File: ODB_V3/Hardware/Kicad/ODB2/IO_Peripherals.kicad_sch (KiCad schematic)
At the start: 22 parts, among them J3 SYS_SW_Conn_01x05_Header, J5 RFM_Conn_Coaxial, J6 RFD_Conn_01x05_Header, U10 W25Q512JVEIQ, U9 RFM22B

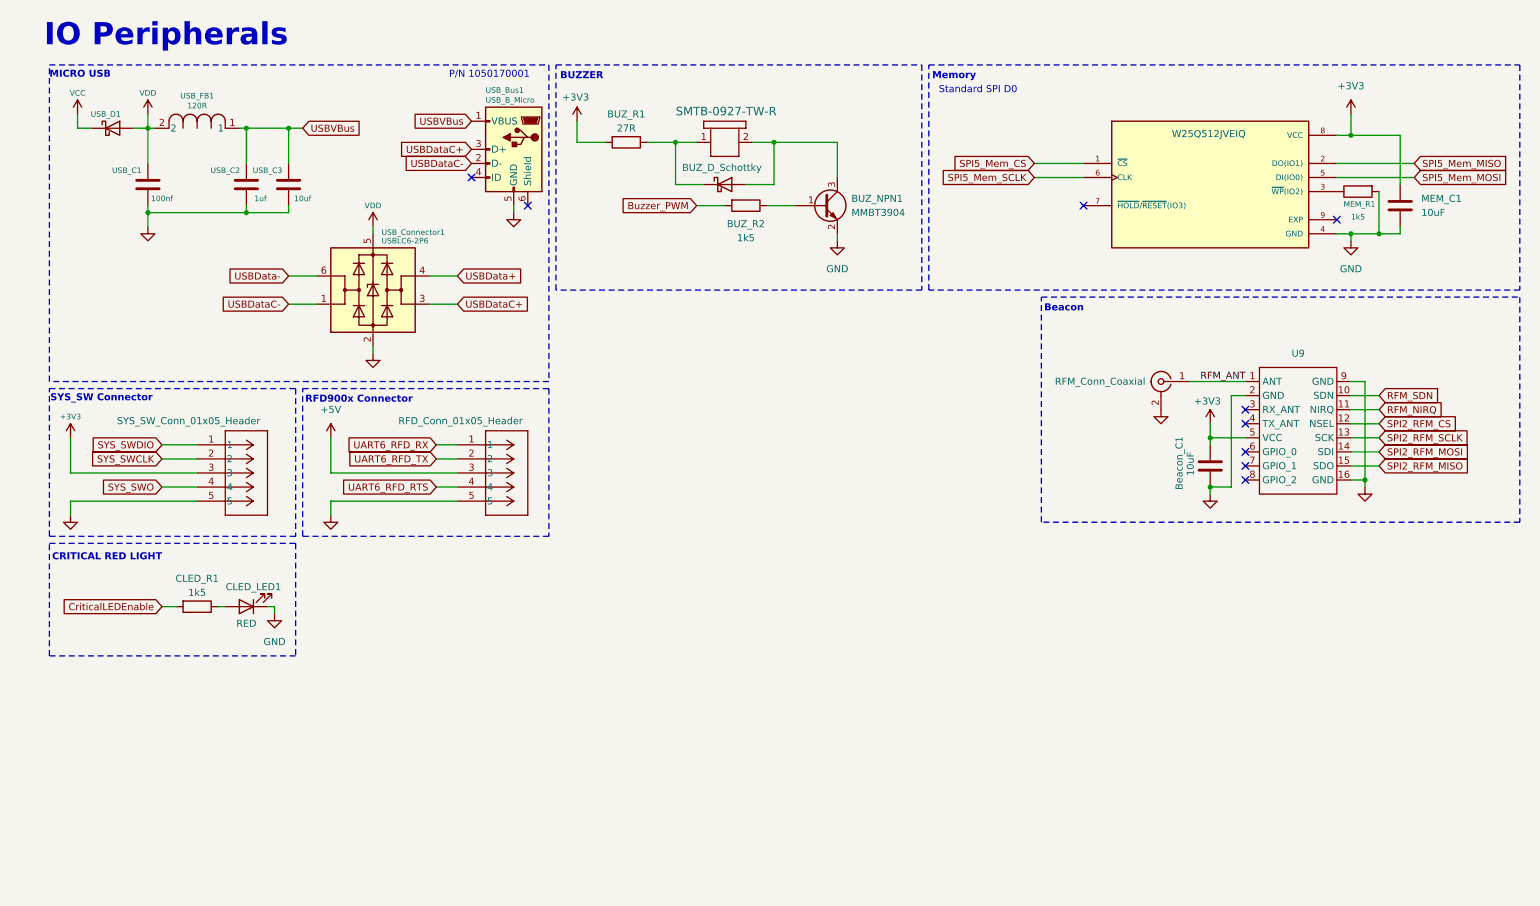
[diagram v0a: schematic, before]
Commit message: feat: new psu design from 5v-36v to 5v (not final)
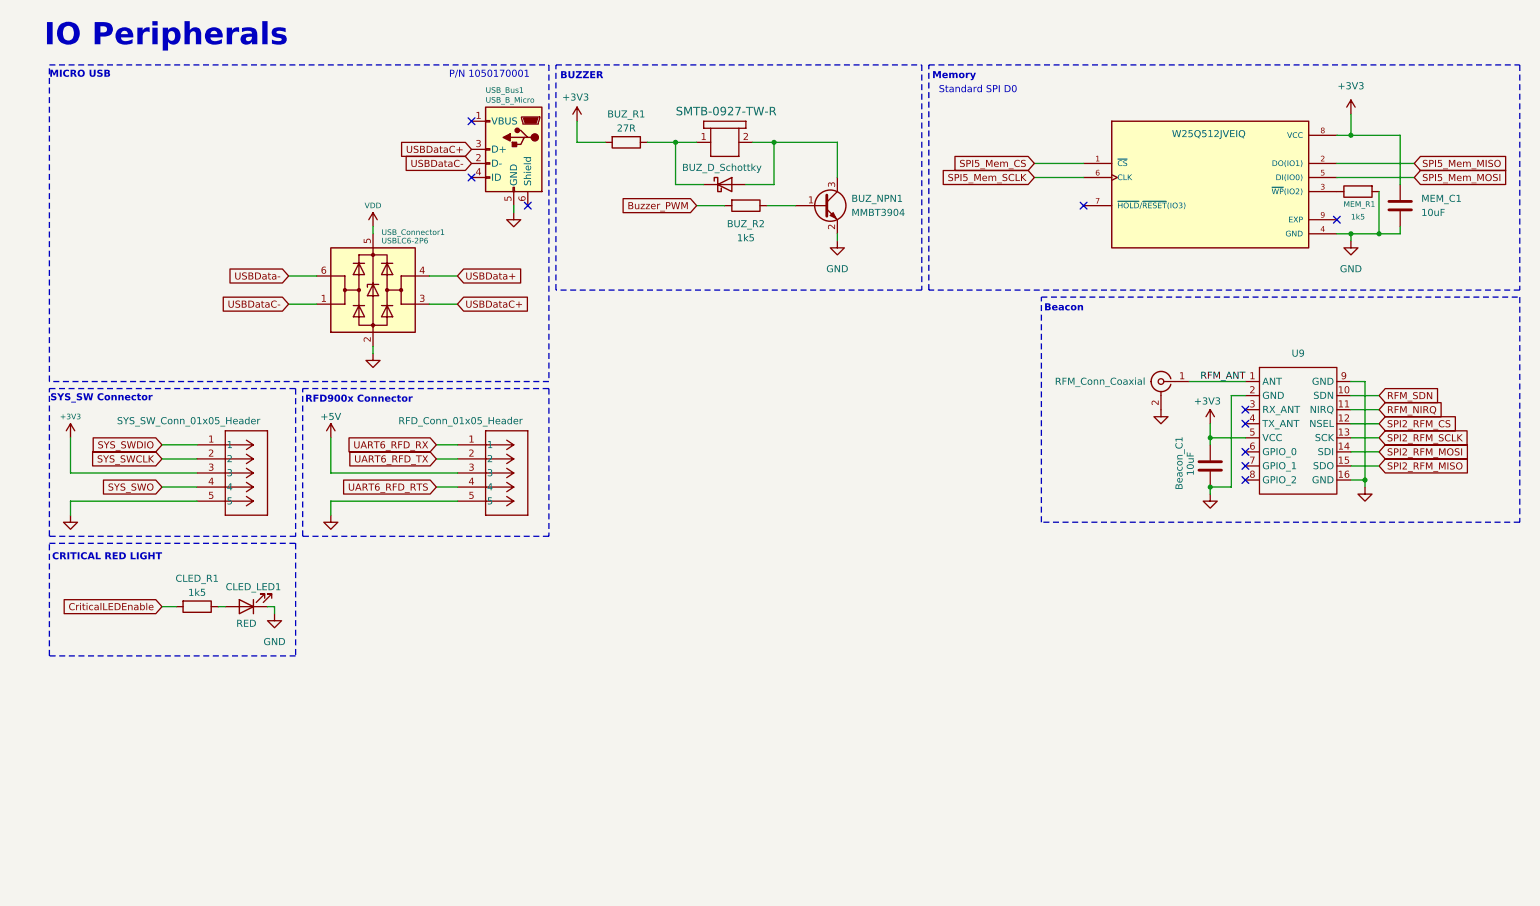
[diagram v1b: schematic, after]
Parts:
- removed USB_C1: 100nf, Capacitor_SMD:C_0603_1608Metric, symbol Device:C
- removed USB_C2: 1uf, Capacitor_SMD:C_0603_1608Metric, symbol Device:C
- removed USB_C3: 10uf, Capacitor_SMD:C_0603_1608Metric, symbol Device:C
- removed USB_D1: B260A-13-F, Diode_SMD:D_SOD-123, symbol Device:D_Schottky
- removed USB_FB1: 120R, IND_25_0805_FRT, symbol ODB2:2508051217Y6
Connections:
- net USBVBus: no longer names the net of USB_Bus1.1 (VBUS)
- no-connect marks 9 -> 10

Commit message: feat!: cleanup components, add new footprint/step, add stm32cubeide conf, start schematics
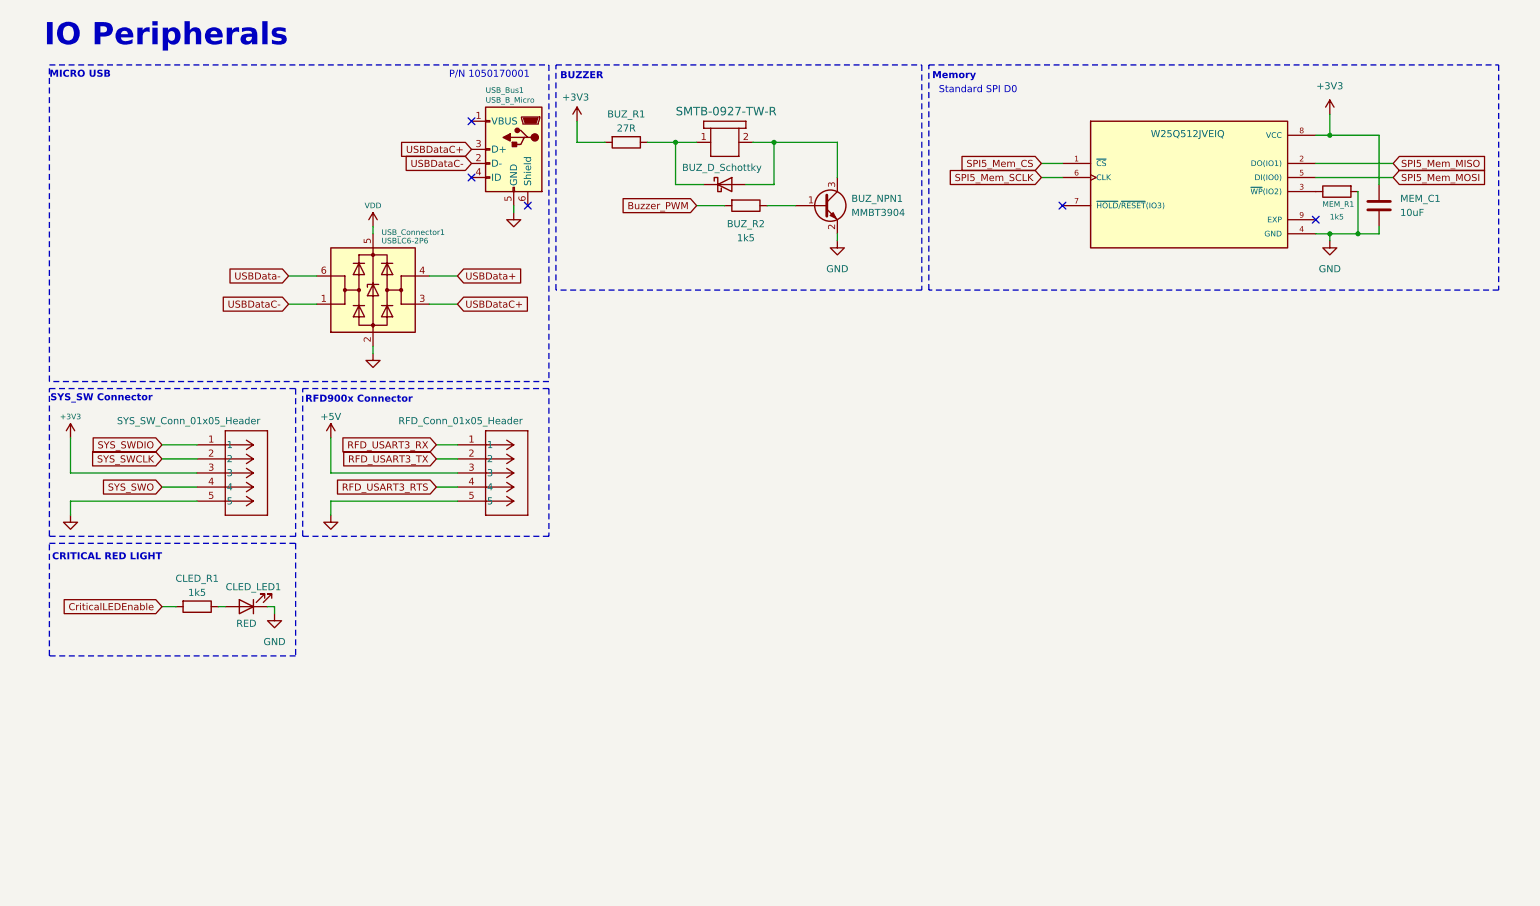
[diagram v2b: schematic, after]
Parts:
- removed Beacon_C1: 10uF, Capacitor_SMD:C_0603_1608Metric, symbol Device:C
- removed J5: RFM_Conn_Coaxial, Connector_Coaxial:SMA_Wurth_60312002114503_Vertical, symbol Connector:Conn_Coaxial
- removed U9: RFM22B, ODB:RFM22b-S2, symbol ODB2:RFM22B-S2
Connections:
- net UART6_RFD_RTS renamed RFD_USART3_RTS
- net UART6_RFD_RX renamed RFD_USART3_RX
- net UART6_RFD_TX renamed RFD_USART3_TX
- no-connect marks 10 -> 5
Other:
- note removed: "Beacon"
- moved on the sheet: MEM_C1, MEM_R1

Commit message: feat: change memory spi to quad spi
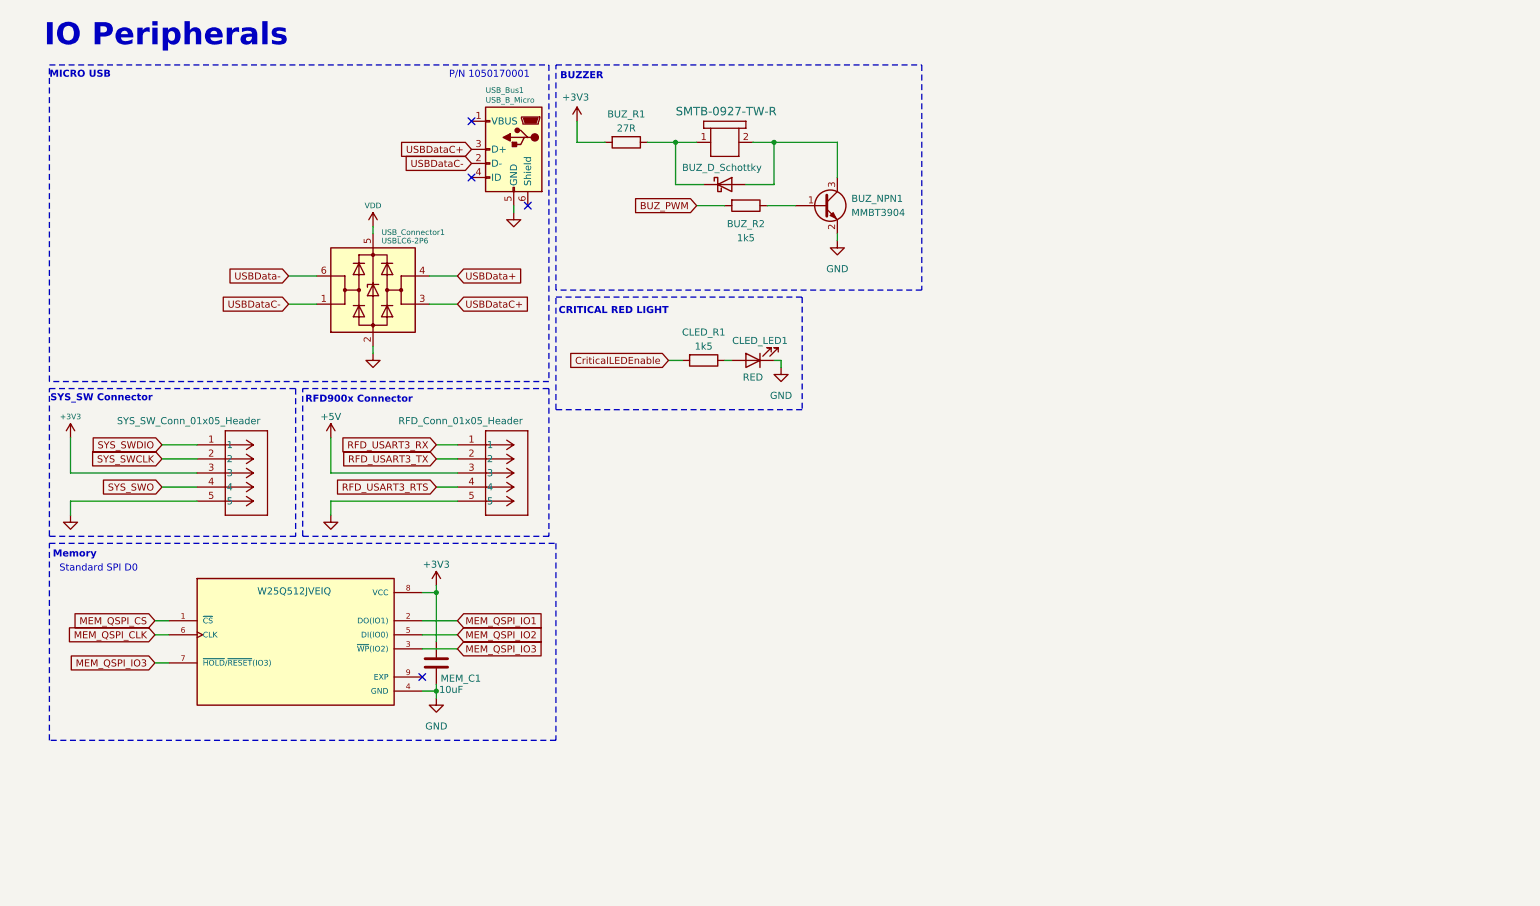
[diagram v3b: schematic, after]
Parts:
- removed MEM_R1: 1k5, Resistor_SMD:R_0603_1608Metric, symbol Device:R
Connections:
- net MEM_QSPI_IO3: now reaches U10.3 (~{WP}(IO2))
- net MEM_QSPI_IO3: now also U10.7 (~{HOLD}/~{RESET}(IO3))
- net Buzzer_PWM renamed BUZ_PWM
- net SPI5_Mem_CS renamed MEM_QSPI_CS
- net SPI5_Mem_MISO renamed MEM_QSPI_IO1
- net SPI5_Mem_MOSI renamed MEM_QSPI_IO2
- net SPI5_Mem_SCLK renamed MEM_QSPI_CLK
- no-connect marks 5 -> 4
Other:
- moved on the sheet: CLED_LED1, CLED_R1, MEM_C1

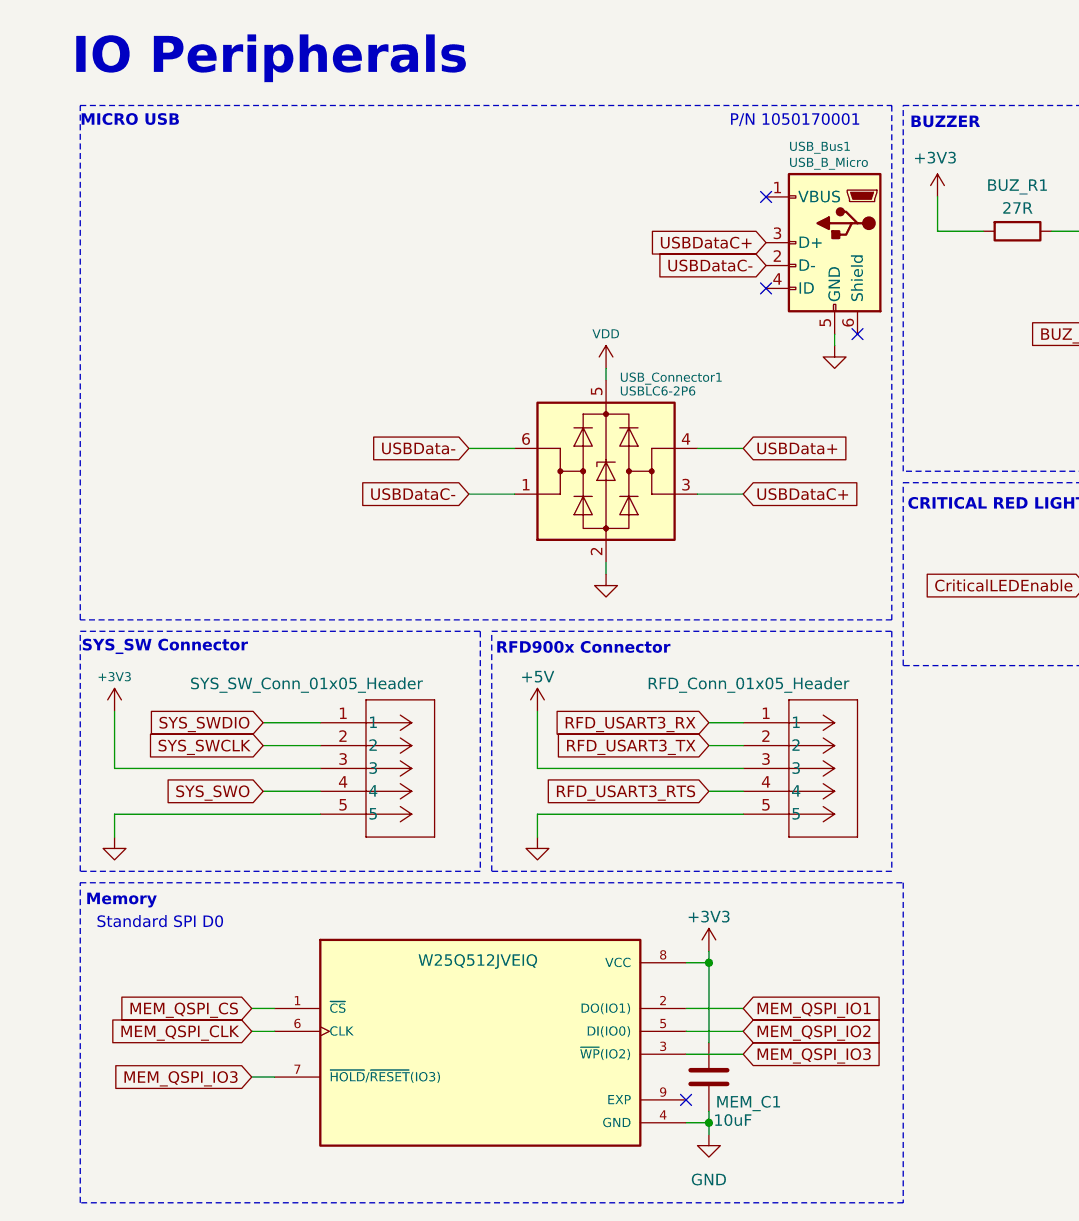
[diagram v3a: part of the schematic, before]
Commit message: feat: add W25Q512JVEIQ + add ZED-F9P-15B
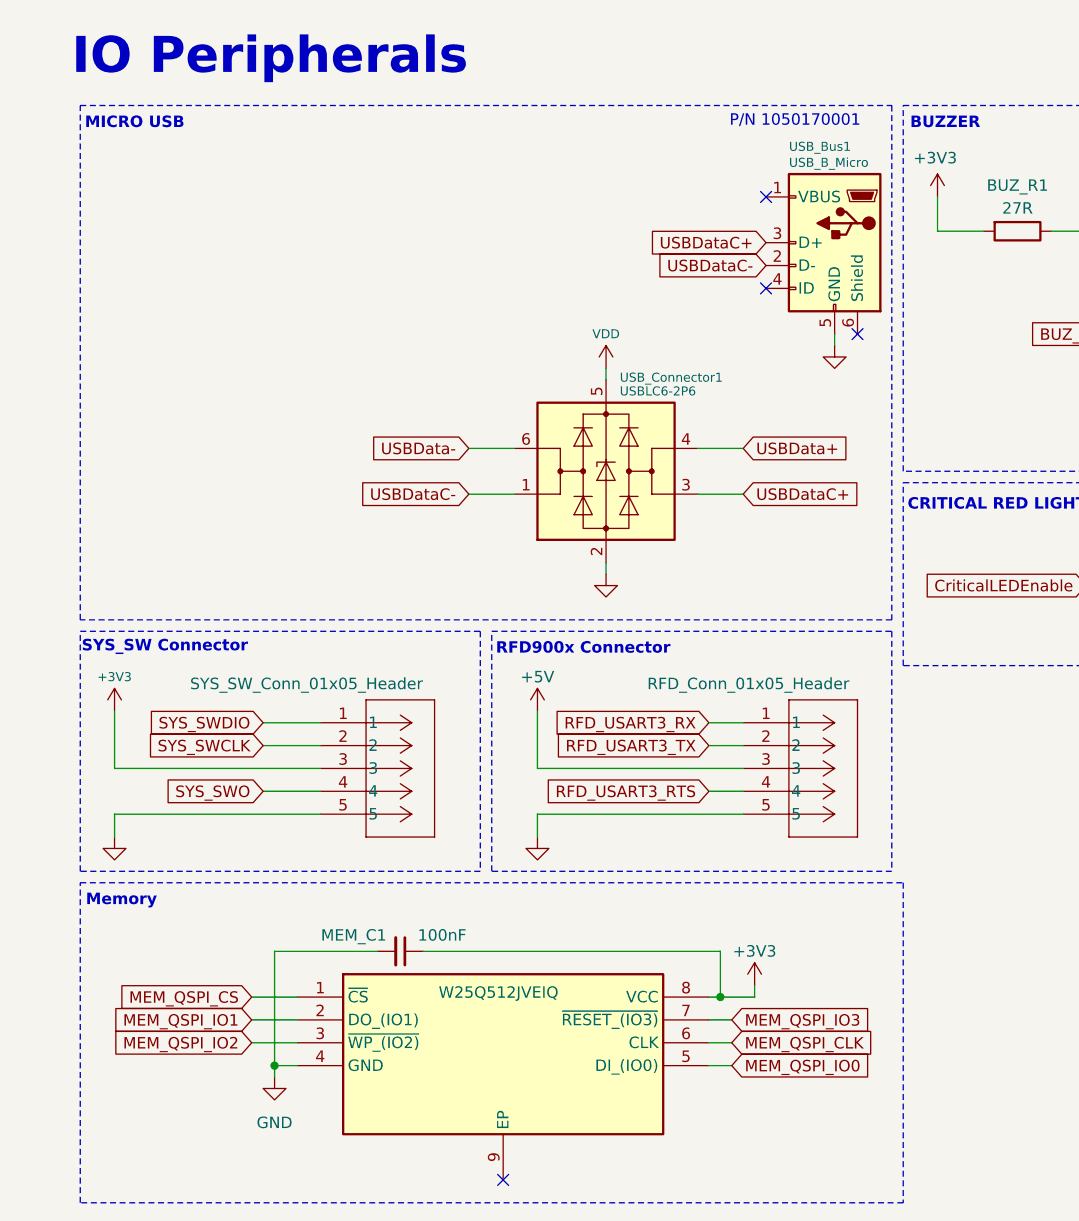
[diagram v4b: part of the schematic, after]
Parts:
- removed MEM_C1: 10uF, Capacitor_SMD:C_0603_1608Metric, symbol Device:C
- removed U10: W25Q512JVEIQ, Library:SON127P600X800X80-9N, symbol ODB_Lib:W25Q512JVEIQ
- added IC1: W25Q512JVEIQ, SON127P800X600X80-9N-D, symbol ODB2:W25Q512JVEIQ
- added MEM_C1: 100nF, Capacitor_SMD:C_0603_1608Metric, symbol Device:C_Small
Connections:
- net +3V3: now also IC1.8 (VCC), MEM_C1.1
- net GND: now also IC1.4 (GND), MEM_C1.2
- net MEM_QSPI_CLK: now also IC1.6 (CLK)
- net MEM_QSPI_CS: now also IC1.1 (~{CS})
- net MEM_QSPI_IO1: now also IC1.2 (DO_(IO1))
- net MEM_QSPI_IO2: now also IC1.3 (~{WP_(IO2)})
- net MEM_QSPI_IO3: now also IC1.7 (~{RESET_(IO3)})
- new net MEM_QSPI_IO0: IC1.5 (DI_(IO0))
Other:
- note removed: "Standard SPI D0"
